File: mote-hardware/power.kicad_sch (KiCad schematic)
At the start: 11 parts, among them J1 USB_C_Receptacle_USB2.0_14P, U2 NCP1117-3.3_SOT223

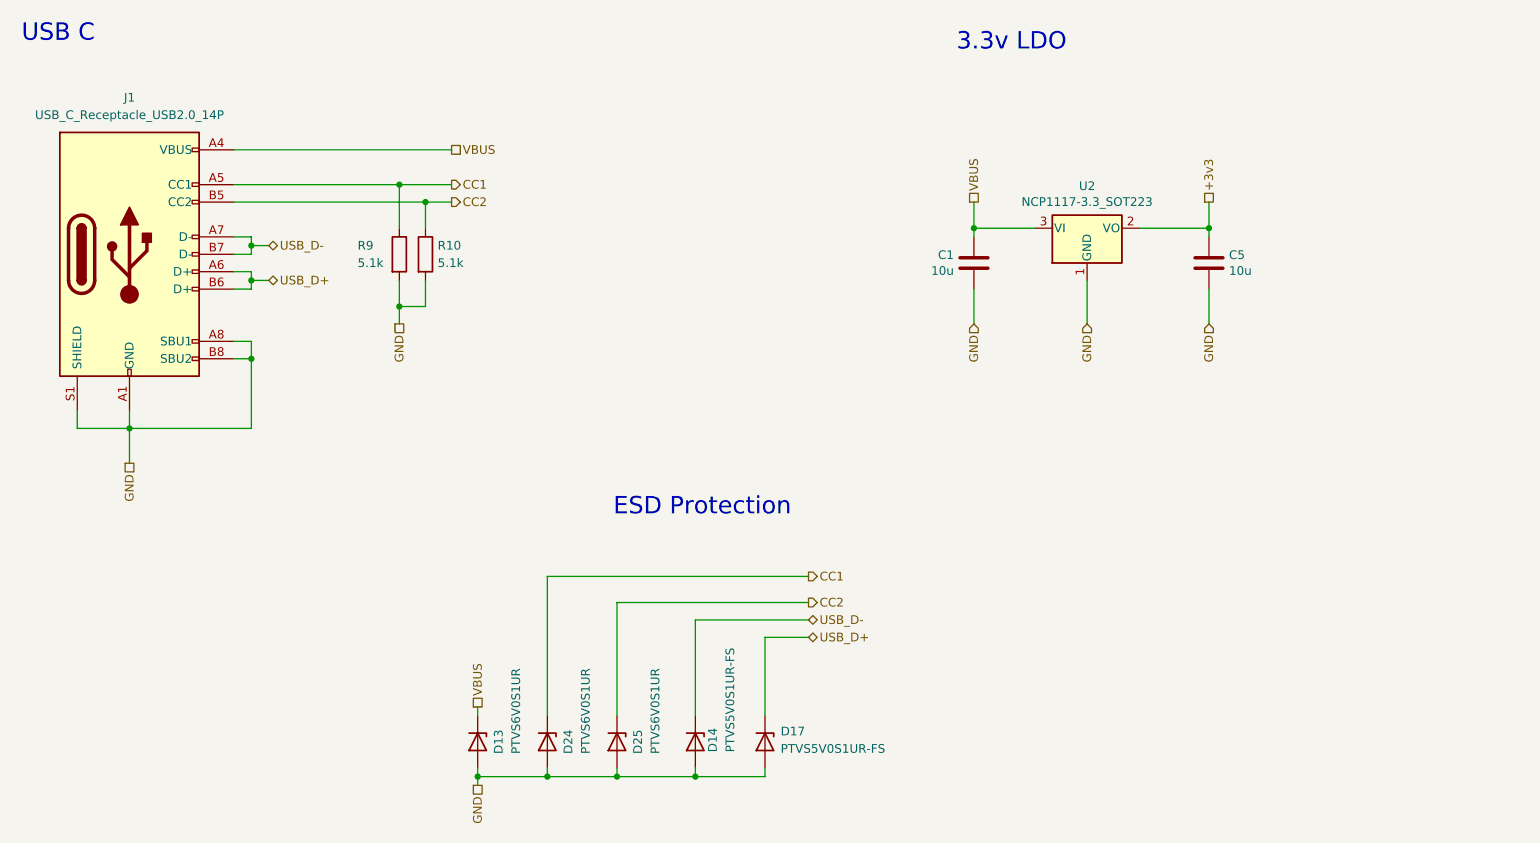
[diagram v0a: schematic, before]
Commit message: mote-hardware v0.2.0 (#63)
Improvements to the pcb design for rev v0.2.0
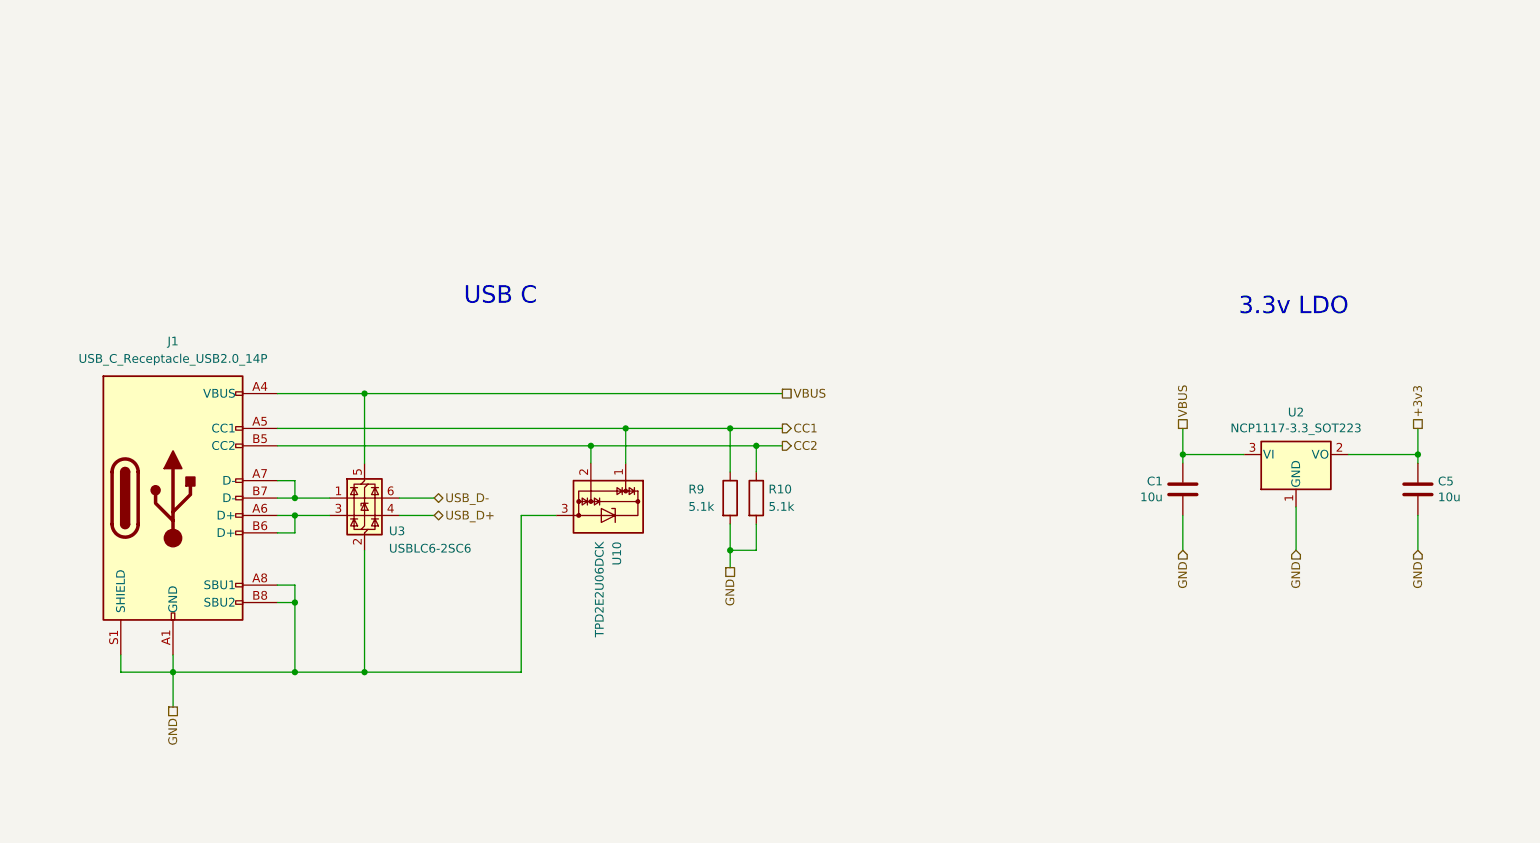
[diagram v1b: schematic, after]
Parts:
- removed D13, D24, D25: PTVS6V0S1UR, Diode_SMD:D_SOD-123, symbol Diode:PTVS7V5Z1USK
- removed D14, D17: PTVS5V0S1UR-FS, Diode_SMD:D_SOD-123, symbol Diode:PTVS5V0Z1USK
- added U10: TPD2E2U06DCK, Package_TO_SOT_SMD:SOT-323_SC-70, symbol Power_Protection:TPD2E2U06DCK
- added U3: USBLC6-2SC6, Package_TO_SOT_SMD:SOT-23-6, symbol Power_Protection:USBLC6-2SC6
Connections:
- net CC1: now also U10.1
- net CC2: now also U10.2
- net GND: now also U10.3, U3.2 (GND)
- net USB_D+: now also U3.4 (I/O2); no longer J1.A6 (D+), J1.B6 (D+)
- net USB_D-: now also U3.6 (I/O1); no longer J1.A7 (D-), J1.B7 (D-)
- net VBUS: now also U3.5 (VBUS)
- new net: J1.A6 (D+), J1.B6 (D+), U3.3 (I/O2)
- new net: J1.A7 (D-), J1.B7 (D-), U3.1 (I/O1)
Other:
- note removed: "ESD Protection"
- company: github.com/empriselab/mote-core -> github.com/empriselab/mote
- moved on the sheet: C1, C5, J1, R10, R9, U2

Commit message: Small tweaks and fixes to the schematic (#68)
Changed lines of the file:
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@@
 	(title_block
 		(title "Mote")
-		(date "2026-05-25")
+		(date "2026-06-07")
 		(rev "V0.2.0")
 		(company "github.com/empriselab/mote")
@@
 			)
 		)
-		(property "Description" ""
-			(at 233.68 99.06 0)
+		(property "Description" "1A Low drop-out regulator, Fixed Output 3.3V, SOT-223"
+			(at 234.188 85.09 0)
 			(effects
 				(font

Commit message: Update postition and rotation values for new components (#69)
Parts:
- U10, U3: JLCPCB_CORRECTION 0; 0; 0 -> 0; 0; -90
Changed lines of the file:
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@@
 			)
 		)
-		(property "JLCPCB_CORRECTION" "0; 0; 0"
+		(property "JLCPCB_CORRECTION" "0; 0; -90"
 			(at 133.35 107.95 0)
 			(effects
@@
 			)
 		)
-		(property "JLCPCB_CORRECTION" "0; 0; 0"
+		(property "JLCPCB_CORRECTION" "0; 0; -90"
 			(at 97.79 105.41 0)
 			(effects
